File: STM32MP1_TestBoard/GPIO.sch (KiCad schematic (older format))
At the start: 13 parts, among them J1 Conn_01x27, J2 Conn_01x27, J3 Conn_01x27, J4 Conn_01x27, J5 Conn_02x03_Odd_Even, J7 Conn_01x08, U1 STM32MP157xAC

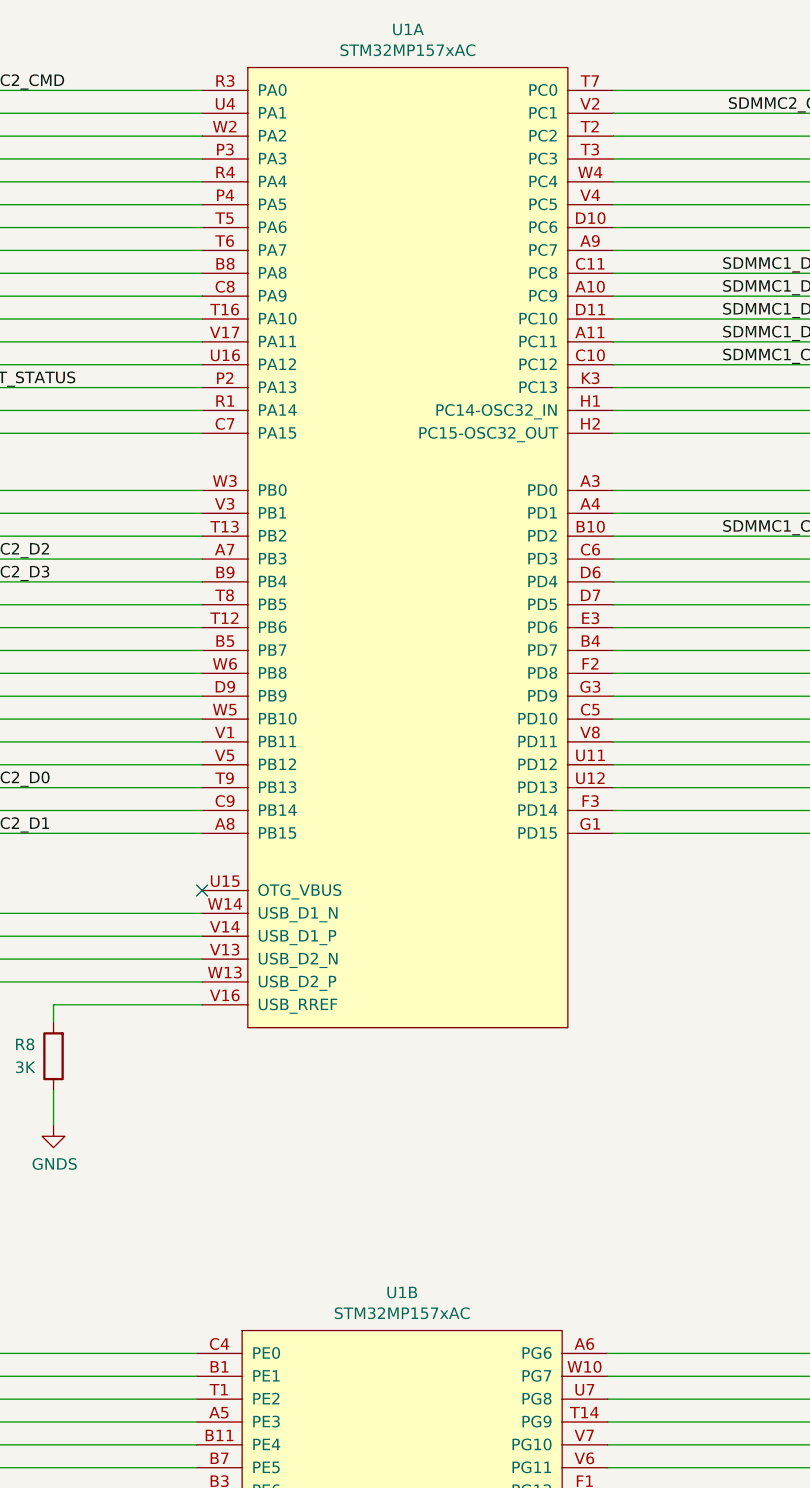
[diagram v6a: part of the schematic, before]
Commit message: corrected STM32MP157 footprint
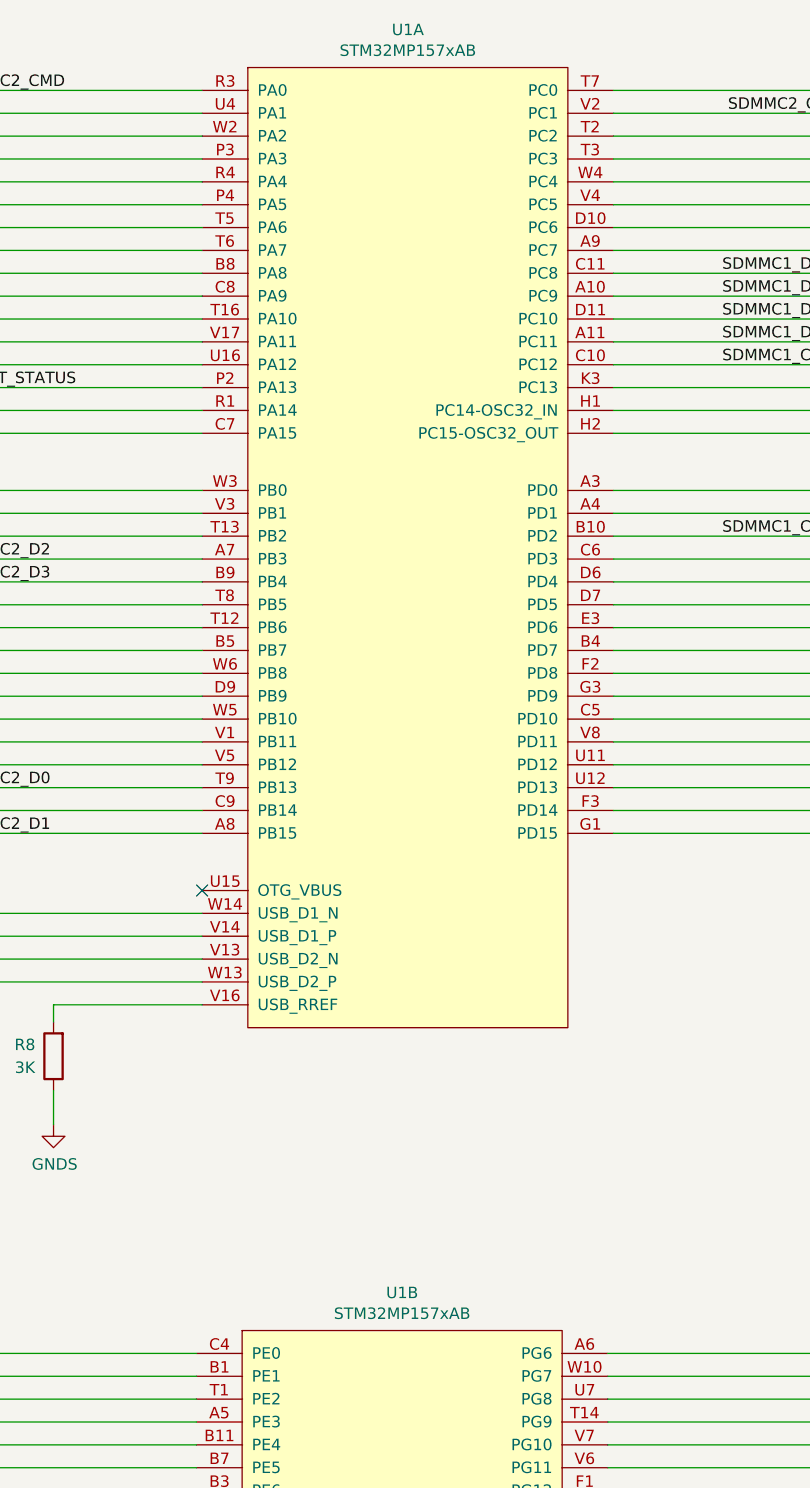
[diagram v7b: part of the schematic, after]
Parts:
- U1: value STM32MP157xAC -> STM32MP157xAB; footprint STM32MP151_LFBGA:BGA-361_19x19_16.0x16.0mm -> STM32MP151_LFBGA:BGA-354_19x19_16.0x16.0mm
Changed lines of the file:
@@
 P 8900 8225
 F 0 "U1" H 8900 9790 50  0000 C CNN
-F 1 "STM32MP157xAC" H 8900 9699 50  0000 C CNN
-F 2 "STM32MP151_LFBGA:BGA-361_19x19_16.0x16.0mm" H 8750 10125 50  0001 C CNN
+F 1 "STM32MP157xAB" H 8900 9699 50  0000 C CNN
+F 2 "STM32MP151_LFBGA:BGA-354_19x19_16.0x16.0mm" H 8750 10125 50  0001 C CNN
 F 3 "https://www.st.com/resource/en/datasheet/stm32mp151c.pdf" H 9550 8375 50  0001 C CNN
 F 4 "~" H 8900 8225 50  0001 C CNN "Mfr"
@@
 P 8875 3300
 F 0 "U1" H 8925 5465 50  0000 C CNN
-F 1 "STM32MP157xAC" H 8925 5374 50  0000 C CNN
-F 2 "STM32MP151_LFBGA:BGA-361_19x19_16.0x16.0mm" H 8725 5200 50  0001 C CNN
+F 1 "STM32MP157xAB" H 8925 5374 50  0000 C CNN
+F 2 "STM32MP151_LFBGA:BGA-354_19x19_16.0x16.0mm" H 8725 5200 50  0001 C CNN
 F 3 "https://www.st.com/resource/en/datasheet/stm32mp151c.pdf" H 9525 3450 50  0001 C CNN
 F 4 "~" H 8875 3300 50  0001 C CNN "Mfr"

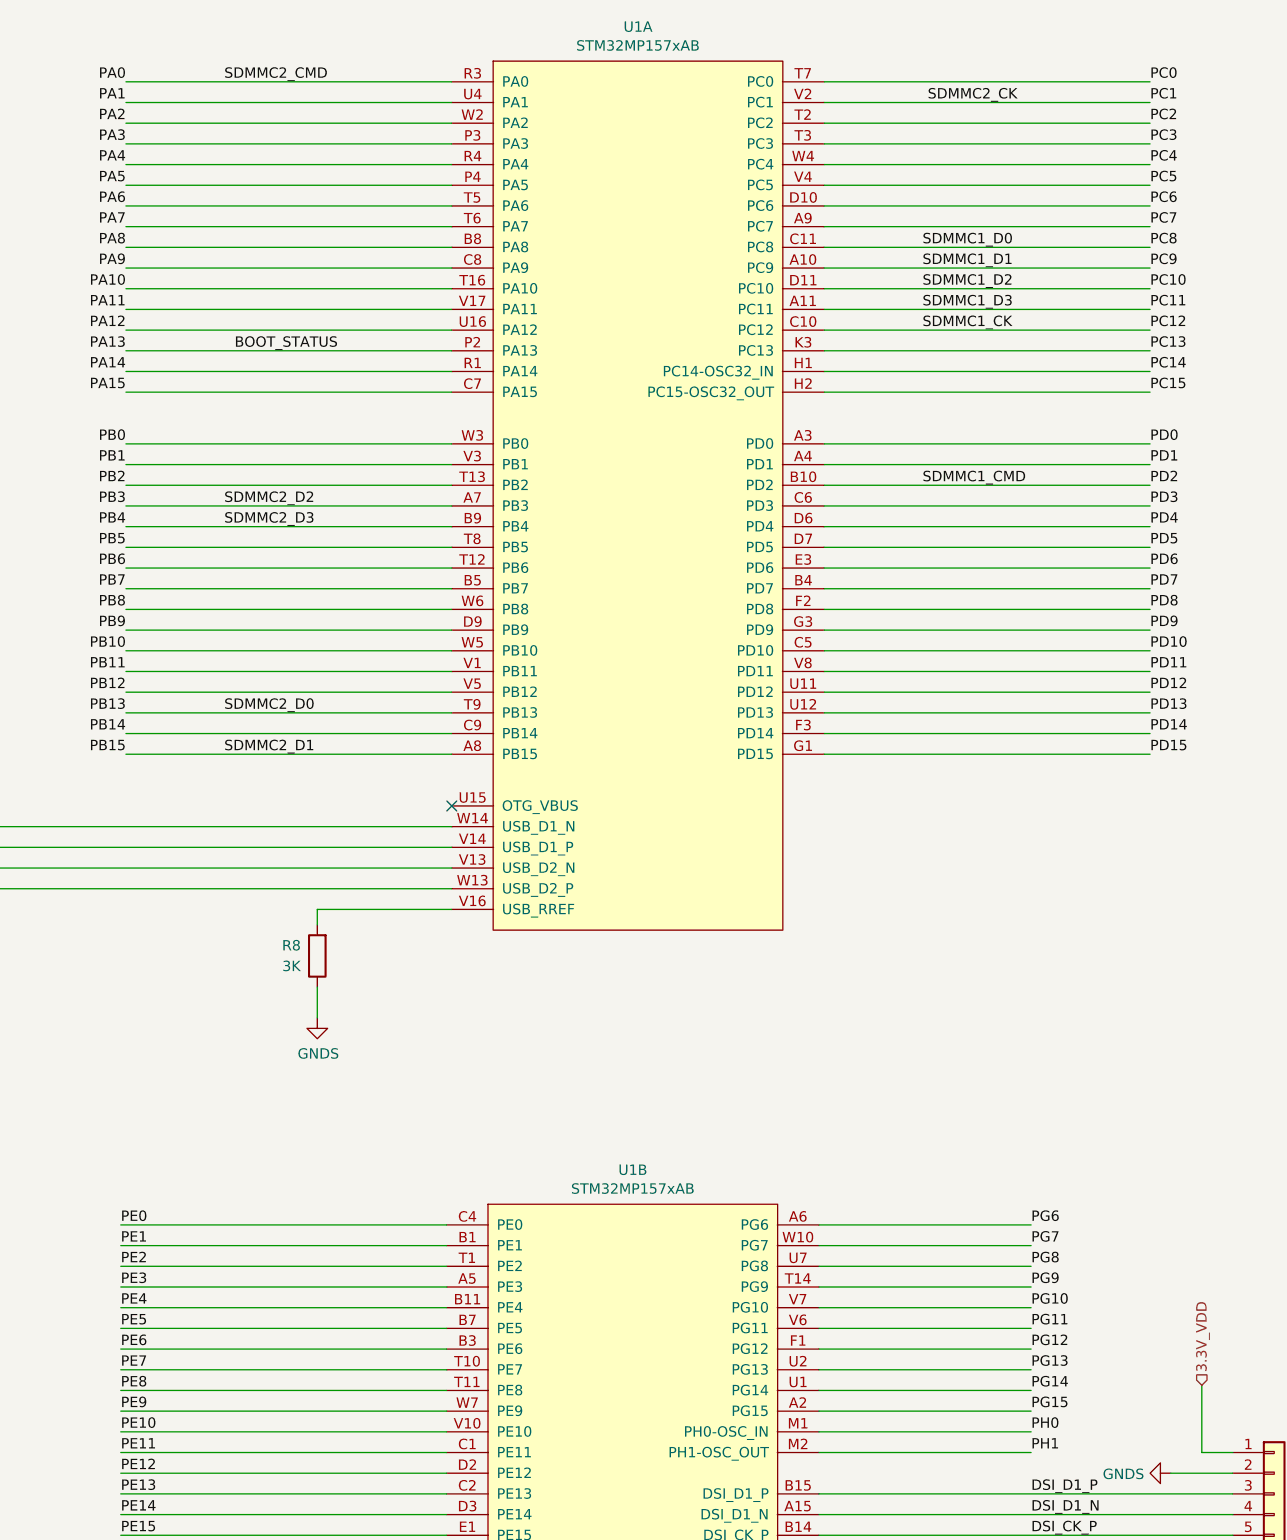
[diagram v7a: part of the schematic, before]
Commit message: added USART tags to GPIO pins on schema
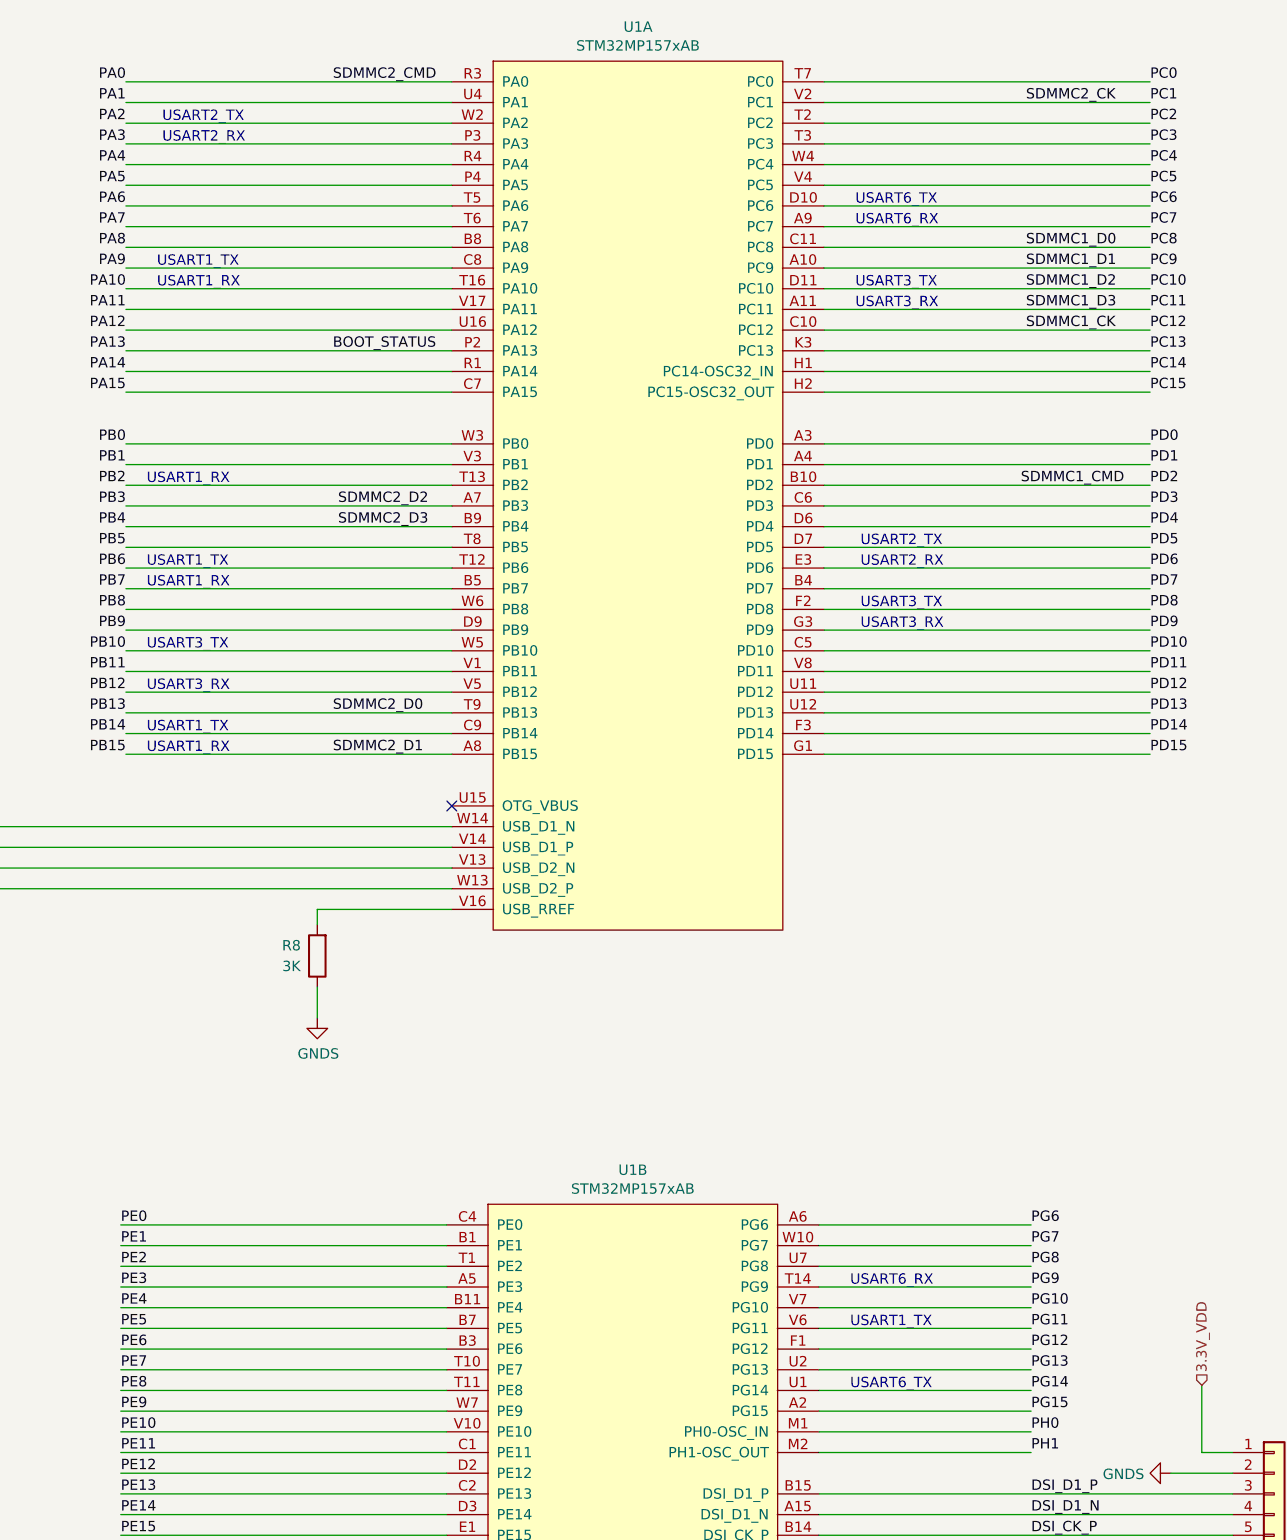
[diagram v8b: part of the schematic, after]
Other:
- note added: "USART1_RX"
- note added: "USART1_TX"
- note added: "USART2_RX"
- note added: "USART2_TX"
- note added: "USART3_RX"
- note added: "USART3_TX"
- note added: "USART6_RX"
- note added: "USART6_TX"
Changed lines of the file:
@@
 F8 "3V3_SDIO_VDD" I R 3675 1525 50
 $EndSheet
-Text Label 6925 1400 0    50   ~ 0
+Text Label 7450 1400 0    50   ~ 0
 SDMMC2_CMD
-Text Label 10325 1500 0    50   ~ 0
+Text Label 10800 1500 0    50   ~ 0
 SDMMC2_CK
-Text Label 10300 2200 0    50   ~ 0
+Text Label 10800 2200 0    50   ~ 0
 SDMMC1_D0
 Text Label 4500 2025 2    50   ~ 0
@@
 Text Label 4500 2325 2    50   ~ 0
 SDMMC1_D3
-Text Label 10300 2300 0    50   ~ 0
+Text Label 10800 2300 0    50   ~ 0
 SDMMC1_D1
-Text Label 10300 2400 0    50   ~ 0
+Text Label 10800 2400 0    50   ~ 0
 SDMMC1_D2
-Text Label 10300 2500 0    50   ~ 0
+Text Label 10800 2500 0    50   ~ 0
 SDMMC1_D3
-Text Label 10300 3350 0    50   ~ 0
+Text Label 10775 3350 0    50   ~ 0
 SDMMC1_CMD
 Text Label 4500 1800 2    50   ~ 0
@@
 Text Label 4500 1700 2    50   ~ 0
 SDMMC1_CK
-Text Label 10300 2600 0    50   ~ 0
+Text Label 10800 2600 0    50   ~ 0
 SDMMC1_CK
-Text Label 6925 3550 0    50   ~ 0
+Text Label 7475 3550 0    50   ~ 0
 SDMMC2_D3
-Text Label 6925 4450 0    50   ~ 0
+Text Label 7450 4450 0    50   ~ 0
 SDMMC2_D0
-Text Label 6925 4650 0    50   ~ 0
+Text Label 7450 4650 0    50   ~ 0
 SDMMC2_D1
-Text Label 6925 3450 0    50   ~ 0
+Text Label 7475 3450 0    50   ~ 0
 SDMMC2_D2
 $Sheet
@@
 Wire Wire Line
 	3475 9525 3900 9525
-Text Label 6975 2700 0    50   ~ 0
+Text Label 7450 2700 0    50   ~ 0
 BOOT_STATUS
 Text Label 8150 10750 0    50   ~ 0
@@
 	0    1    1    0
 $EndComp
+Text Notes 10000 3750 0    50   ~ 0
+USART2_RX
+Text Notes 10000 3950 0    50   ~ 0
+USART3_TX
+Text Notes 10000 4050 0    50   ~ 0
+USART3_RX
+Text Notes 6625 1700 0    50   ~ 0
+USART2_RX
+Text Notes 9950 7725 0    50   ~ 0
+USART6_TX
+Text Notes 6625 1600 0    50   ~ 0
+USART2_TX
+Text Notes 6550 4150 0    50   ~ 0
+USART3_TX
+Text Notes 6550 4350 0    50   ~ 0
+USART3_RX
+Text Notes 9950 7425 0    50   ~ 0
+USART1_TX
+Text Notes 6550 3750 0    50   ~ 0
+USART1_TX
+Text Notes 6550 3350 0    50   ~ 0
+USART1_RX
+Text Notes 9950 7225 0    50   ~ 0
+USART6_RX
+Text Notes 6600 2400 0    50   ~ 0
+USART1_RX
+Text Notes 9975 2500 0    50   ~ 0
+USART3_RX
+Text Notes 9975 2400 0    50   ~ 0
+USART3_TX
+Text Notes 9975 2100 0    50   ~ 0
+USART6_RX
+Text Notes 9975 2000 0    50   ~ 0
+USART6_TX
+Text Notes 6550 4550 0    50   ~ 0
+USART1_TX
+Text Notes 6550 4650 0    50   ~ 0
+USART1_RX
+Text Notes 6600 2300 0    50   ~ 0
+USART1_TX
+Text Notes 6550 3850 0    50   ~ 0
+USART1_RX
+Text Notes 10000 3650 0    50   ~ 0
+USART2_TX
 $EndSCHEMATC
